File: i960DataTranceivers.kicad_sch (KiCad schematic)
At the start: 6 parts

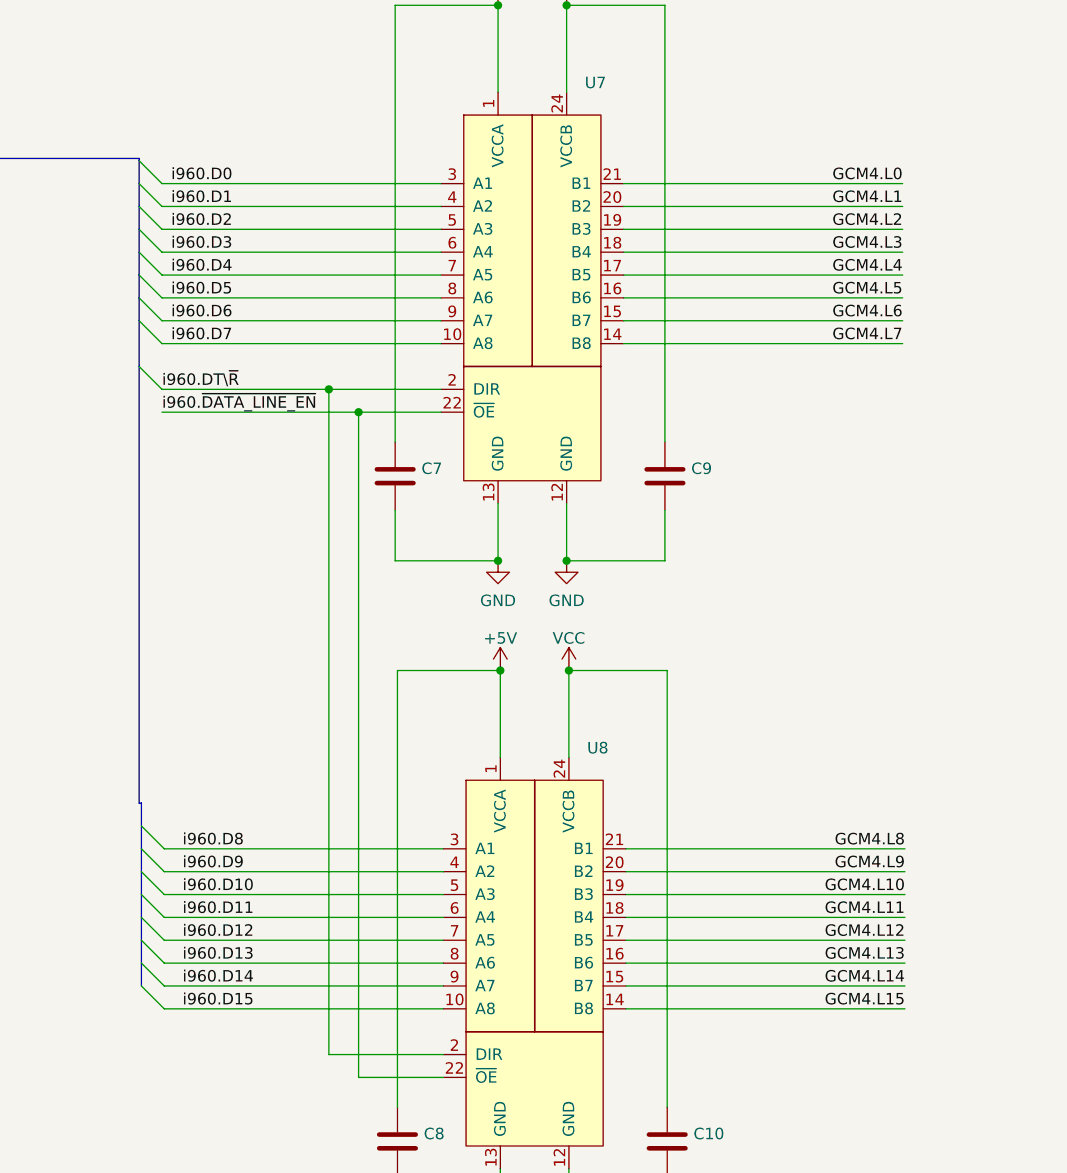
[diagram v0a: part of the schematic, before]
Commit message: Added a metro m4 connector
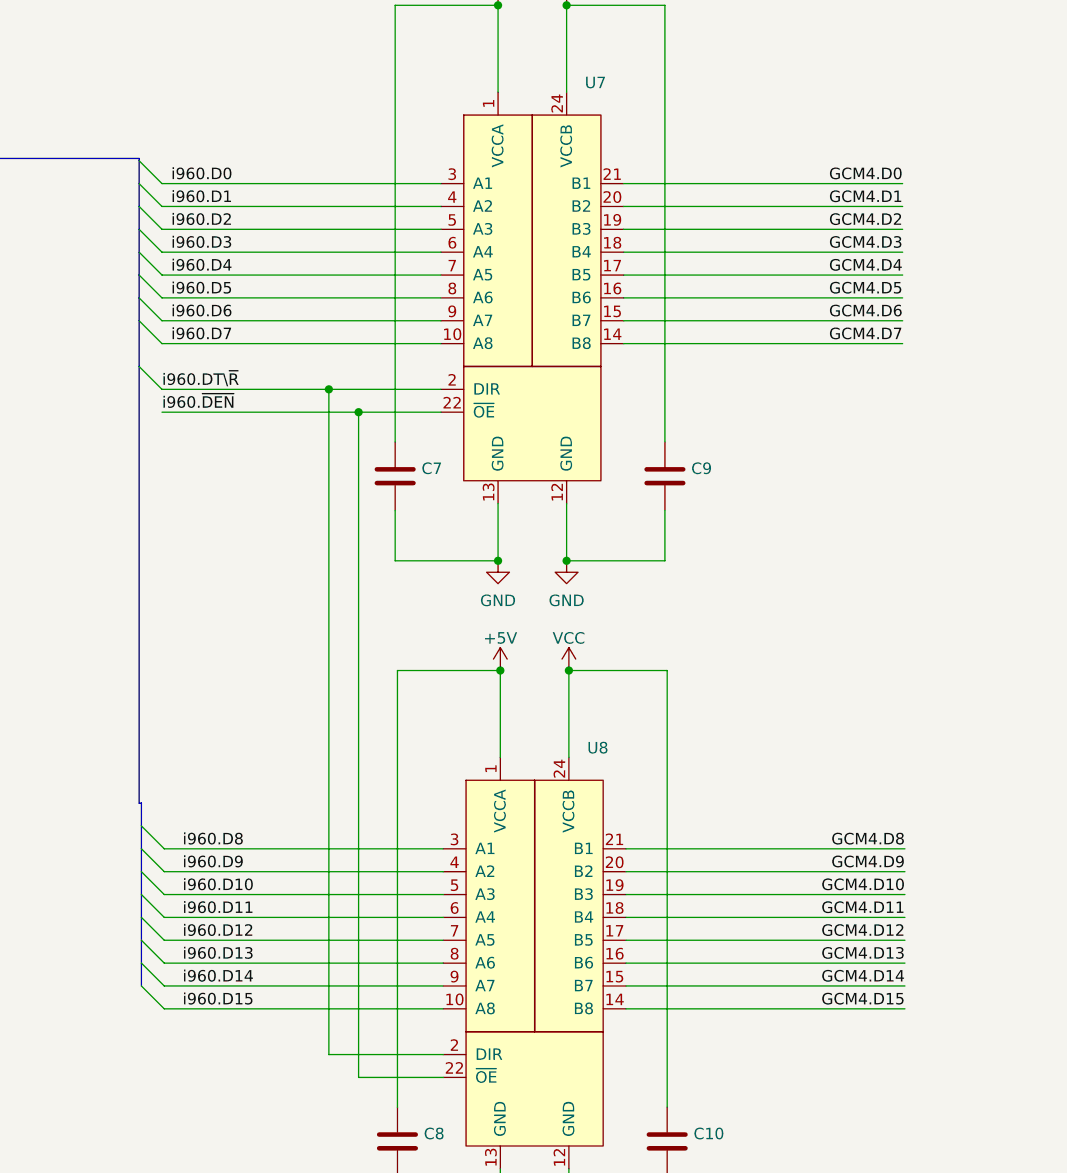
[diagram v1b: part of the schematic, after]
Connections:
- net GCM4.L0 renamed GCM4.D0
- net GCM4.L1 renamed GCM4.D1
- net GCM4.L10 renamed GCM4.D10
- net GCM4.L11 renamed GCM4.D11
- net GCM4.L12 renamed GCM4.D12
- net GCM4.L13 renamed GCM4.D13
- net GCM4.L14 renamed GCM4.D14
- net GCM4.L15 renamed GCM4.D15
- net GCM4.L2 renamed GCM4.D2
- net GCM4.L3 renamed GCM4.D3
- net GCM4.L4 renamed GCM4.D4
- net GCM4.L5 renamed GCM4.D5
- net GCM4.L6 renamed GCM4.D6
- net GCM4.L7 renamed GCM4.D7
- net GCM4.L8 renamed GCM4.D8
- net GCM4.L9 renamed GCM4.D9
- net i960.~{DATA_LINE_EN} renamed i960.~{DEN}
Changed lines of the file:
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@@
     (effects (font (size 1.27 1.27)) (justify left bottom))
   )
-  (label "GCM4.L9" (at 168.148 121.412 180)
-    (effects (font (size 1.27 1.27)) (justify right bottom))
-  )
-  (label "GCM4.L3" (at 167.894 52.578 180)
+  (label "GCM4.D13" (at 168.148 131.572 180)
     (effects (font (size 1.27 1.27)) (justify right bottom))
   )
   (label "i960.D1" (at 86.614 47.498 0)
     (effects (font (size 1.27 1.27)) (justify left bottom))
-  )
-  (label "GCM4.L13" (at 168.148 131.572 180)
-    (effects (font (size 1.27 1.27)) (justify right bottom))
-  )
-  (label "GCM4.L15" (at 168.148 136.652 180)
-    (effects (font (size 1.27 1.27)) (justify right bottom))
-  )
-  (label "i960.~{DATA_LINE_EN}" (at 85.598 70.358 0)
-    (effects (font (size 1.27 1.27)) (justify left bottom))
-  )
-  (label "GCM4.L7" (at 167.894 62.738 180)
-    (effects (font (size 1.27 1.27)) (justify right bottom))
   )
   (label "i960.D11" (at 87.884 126.492 0)
@@
     (effects (font (size 1.27 1.27)) (justify left bottom))
   )
-  (label "GCM4.L6" (at 167.894 60.198 180)
+  (label "GCM4.D1" (at 167.894 47.498 180)
     (effects (font (size 1.27 1.27)) (justify right bottom))
   )
   (label "i960.D0" (at 86.614 44.958 0)
     (effects (font (size 1.27 1.27)) (justify left bottom))
-  )
-  (label "GCM4.L1" (at 167.894 47.498 180)
-    (effects (font (size 1.27 1.27)) (justify right bottom))
   )
   (label "i960.D5" (at 86.614 57.658 0)
@@
     (effects (font (size 1.27 1.27)) (justify left bottom))
   )
-  (label "GCM4.L12" (at 168.148 129.032 180)
-    (effects (font (size 1.27 1.27)) (justify right bottom))
-  )
-  (label "GCM4.L10" (at 168.148 123.952 180)
+  (label "GCM4.D7" (at 167.894 62.738 180)
     (effects (font (size 1.27 1.27)) (justify right bottom))
   )
@@
     (effects (font (size 1.27 1.27)) (justify left bottom))
   )
-  (label "GCM4.L14" (at 168.148 134.112 180)
-    (effects (font (size 1.27 1.27)) (justify right bottom))
-  )
   (label "i960.D8" (at 87.884 118.872 0)
     (effects (font (size 1.27 1.27)) (justify left bottom))
   )
+  (label "GCM4.D4" (at 167.894 55.118 180)
+    (effects (font (size 1.27 1.27)) (justify right bottom))
+  )
+  (label "GCM4.D6" (at 167.894 60.198 180)
+    (effects (font (size 1.27 1.27)) (justify right bottom))
+  )
+  (label "GCM4.D3" (at 167.894 52.578 180)
+    (effects (font (size 1.27 1.27)) (justify right bottom))
+  )
   (label "i960.D2" (at 86.614 50.038 0)
+    (effects (font (size 1.27 1.27)) (justify left bottom))
+  )
+  (label "i960.~{DEN}" (at 85.598 70.358 0)
     (effects (font (size 1.27 1.27)) (justify left bottom))
   )
@@
     (effects (font (size 1.27 1.27)) (justify left bottom))
   )
-  (label "GCM4.L4" (at 167.894 55.118 180)
-    (effects (font (size 1.27 1.27)) (justify right bottom))
-  )
   (label "i960.D15" (at 87.884 136.652 0)
     (effects (font (size 1.27 1.27)) (justify left bottom))
   )
-  (label "GCM4.L5" (at 167.894 57.658 180)
+  (label "GCM4.D12" (at 168.148 129.032 180)
     (effects (font (size 1.27 1.27)) (justify right bottom))
   )
@@
     (effects (font (size 1.27 1.27)) (justify left bottom))
   )
-  (label "GCM4.L11" (at 168.148 126.492 180)
+  (label "GCM4.D0" (at 167.894 44.958 180)
     (effects (font (size 1.27 1.27)) (justify right bottom))
   )
@@
     (effects (font (size 1.27 1.27)) (justify left bottom))
   )
-  (label "GCM4.L0" (at 167.894 44.958 180)
+  (label "GCM4.D9" (at 168.148 121.412 180)
     (effects (font (size 1.27 1.27)) (justify right bottom))
   )
-  (label "GCM4.L2" (at 167.894 50.038 180)
+  (label "GCM4.D8" (at 168.148 118.872 180)
     (effects (font (size 1.27 1.27)) (justify right bottom))
   )
-  (label "GCM4.L8" (at 168.148 118.872 180)
+  (label "GCM4.D5" (at 167.894 57.658 180)
     (effects (font (size 1.27 1.27)) (justify right bottom))
   )
@@
     (effects (font (size 1.27 1.27)) (justify left bottom))
   )
+  (label "GCM4.D11" (at 168.148 126.492 180)
+    (effects (font (size 1.27 1.27)) (justify right bottom))
+  )
   (label "i960.D10" (at 87.884 123.952 0)
     (effects (font (size 1.27 1.27)) (justify left bottom))
+  )
+  (label "GCM4.D10" (at 168.148 123.952 180)
+    (effects (font (size 1.27 1.27)) (justify right bottom))
+  )
+  (label "GCM4.D2" (at 167.894 50.038 180)
+    (effects (font (size 1.27 1.27)) (justify right bottom))
+  )
+  (label "GCM4.D14" (at 168.148 134.112 180)
+    (effects (font (size 1.27 1.27)) (justify right bottom))
   )
   (label "i960.DT\\~{R}" (at 85.598 67.818 0)
@@
     (effects (font (size 1.27 1.27)) (justify left bottom))
   )
+  (label "GCM4.D15" (at 168.148 136.652 180)
+    (effects (font (size 1.27 1.27)) (justify right bottom))
+  )
   (hierarchical_label "GCM4{CHIPSET}" (shape passive) (at 261.874 19.05 0)

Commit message: Correct the feather symbol and breakouts
Also fix the VCC pin being bound to +5V for some reason. Use VCCIO
instead
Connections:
- net VCC renamed VCCB
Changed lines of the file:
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@@
   (junction (at 107.442 70.358) (diameter 0) (color 0 0 0 0)
   )
+  (junction (at 130.81 160.782) (diameter 0) (color 0 0 0 0)
+  )
+  (junction (at 122.936 86.868) (diameter 0) (color 0 0 0 0)
+  )
+  (junction (at 123.19 160.782) (diameter 0) (color 0 0 0 0)
+  )
+  (junction (at 104.14 67.818) (diameter 0) (color 0 0 0 0)
+  )
+  (junction (at 130.556 25.146) (diameter 0) (color 0 0 0 0)
+  )
+  (junction (at 123.19 99.06) (diameter 0) (color 0 0 0 0)
+  )
   (junction (at 130.81 99.06) (diameter 0) (color 0 0 0 0)
-  )
-  (junction (at 130.81 160.782) (diameter 0) (color 0 0 0 0)
-  )
-  (junction (at 122.936 86.868) (diameter 0) (color 0 0 0 0)
-  )
-  (junction (at 123.19 160.782) (diameter 0) (color 0 0 0 0)
-  )
-  (junction (at 104.14 67.818) (diameter 0) (color 0 0 0 0)
-  )
-  (junction (at 123.19 99.06) (diameter 0) (color 0 0 0 0)
-  )
-  (junction (at 130.556 25.146) (diameter 0) (color 0 0 0 0)
   )
   (junction (at 130.556 86.868) (diameter 0) (color 0 0 0 0)
@@
     (pin "1")
   )
-  (symbol (lib_id "power:VCC") (at 130.81 99.06 0) (unit 1)
-    (in_bom yes) (on_board yes) (fields_autoplaced)
-    (property "Reference" "#PWR0124" (id 0) (at 130.81 102.87 0)
-      (effects (font (size 1.27 1.27)) hide)
-    )
-    (property "Value" "VCC" (id 1) (at 130.81 95.4842 0))
-    (property "Footprint" "" (id 2) (at 130.81 99.06 0)
-      (effects (font (size 1.27 1.27)) hide)
-    )
-    (property "Datasheet" "" (id 3) (at 130.81 99.06 0)
-      (effects (font (size 1.27 1.27)) hide)
-    )
-    (pin "1")
-  )
   (symbol (lib_id "power:+5V") (at 123.19 99.06 0) (unit 1)
     (in_bom yes) (on_board yes) (fields_autoplaced)
@@
     (pin "2")
   )
-  (symbol (lib_id "power:VCC") (at 130.556 25.146 0) (unit 1)
-    (in_bom yes) (on_board yes) (fields_autoplaced)
-    (property "Reference" "#PWR0118" (id 0) (at 130.556 28.956 0)
-      (effects (font (size 1.27 1.27)) hide)
-    )
-    (property "Value" "VCC" (id 1) (at 130.556 21.5702 0))
-    (property "Footprint" "" (id 2) (at 130.556 25.146 0)
-      (effects (font (size 1.27 1.27)) hide)
+  (symbol (lib_id "SparkFun-PowerSymbols:VCCIO") (at 130.556 25.146 0) (unit 1)
+    (in_bom yes) (on_board yes) (fields_autoplaced)
+    (property "Reference" "#SUPPLY0104" (id 0) (at 131.826 25.146 0)
+      (effects (font (size 1.143 1.143)) (justify left bottom) hide)
+    )
+    (property "Value" "" (id 1) (at 130.556 18.8643 0)
+      (effects (font (size 1.143 1.143)))
+    )
+    (property "Footprint" "" (id 2) (at 130.556 21.5153 0)
+      (effects (font (size 1.524 1.524)))
     )
     (property "Datasheet" "" (id 3) (at 130.556 25.146 0)
-      (effects (font (size 1.27 1.27)) hide)
-    )
-    (pin "1")
+      (effects (font (size 1.524 1.524)) hide)
+    )
+    (pin "~")
+  )
+  (symbol (lib_id "SparkFun-PowerSymbols:VCCIO") (at 130.81 99.06 0) (unit 1)
+    (in_bom yes) (on_board yes) (fields_autoplaced)
+    (property "Reference" "#SUPPLY0105" (id 0) (at 132.08 99.06 0)
+      (effects (font (size 1.143 1.143)) (justify left bottom) hide)
+    )
+    (property "Value" "" (id 1) (at 130.81 92.7783 0)
+      (effects (font (size 1.143 1.143)))
+    )
+    (property "Footprint" "" (id 2) (at 130.81 95.4293 0)
+      (effects (font (size 1.524 1.524)))
+    )
+    (property "Datasheet" "" (id 3) (at 130.81 99.06 0)
+      (effects (font (size 1.524 1.524)) hide)
+    )
+    (pin "~")
   )
 )
